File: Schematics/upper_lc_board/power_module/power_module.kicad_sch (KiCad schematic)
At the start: 25 parts, among them U4 PMUX_TPS2121RUXR

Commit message: temp commit for layout work
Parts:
- C10, C12, C13, C9: footprint (none) -> Capacitor_SMD:C_0603_1608Metric
- R11, R12, R25: footprint (none) -> Resistor_SMD:R_0402_1005Metric
- R? (x6): footprint Capacitor_SMD:C_0402_1005Metric -> Resistor_SMD:R_0402_1005Metric
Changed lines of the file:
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@@
 			)
 		)
-		(property "Footprint" ""
+		(property "Footprint" "Capacitor_SMD:C_0603_1608Metric"
 			(at 130.5052 63.5 0)
 			(effects
@@
 			)
 		)
-		(property "Footprint" "Capacitor_SMD:C_0402_1005Metric"
+		(property "Footprint" "Resistor_SMD:R_0402_1005Metric"
 			(at 192.532 139.7 90)
 			(effects
@@
 			)
 		)
-		(property "Footprint" "Capacitor_SMD:C_0402_1005Metric"
+		(property "Footprint" "Resistor_SMD:R_0402_1005Metric"
 			(at 118.618 163.83 90)
 			(effects
@@
 			)
 		)
-		(property "Footprint" "Capacitor_SMD:C_0402_1005Metric"
+		(property "Footprint" "Resistor_SMD:R_0402_1005Metric"
 			(at 192.532 132.08 90)
 			(effects
@@
 			)
 		)
-		(property "Footprint" ""
+		(property "Footprint" "Resistor_SMD:R_0402_1005Metric"
 			(at 123.952 97.79 90)
 			(effects
@@
 			)
 		)
-		(property "Footprint" "Capacitor_SMD:C_0402_1005Metric"
+		(property "Footprint" "Resistor_SMD:R_0402_1005Metric"
 			(at 203.708 124.46 90)
 			(effects
@@
 			)
 		)
-		(property "Footprint" ""
+		(property "Footprint" "Capacitor_SMD:C_0603_1608Metric"
 			(at 137.4648 86.36 0)
 			(effects
@@
 			)
 		)
-		(property "Footprint" "Capacitor_SMD:C_0402_1005Metric"
+		(property "Footprint" "Resistor_SMD:R_0402_1005Metric"
 			(at 118.618 140.97 90)
 			(effects
@@
 			)
 		)
-		(property "Footprint" ""
+		(property "Footprint" "Capacitor_SMD:C_0603_1608Metric"
 			(at 191.4652 63.5 0)
 			(effects
@@
 			)
 		)
-		(property "Footprint" ""
+		(property "Footprint" "Resistor_SMD:R_0402_1005Metric"
 			(at 150.622 92.71 90)
 			(effects
@@
 			)
 		)
-		(property "Footprint" "Capacitor_SMD:C_0402_1005Metric"
+		(property "Footprint" "Resistor_SMD:R_0402_1005Metric"
 			(at 118.618 120.65 90)
 			(effects
@@
 			)
 		)
-		(property "Footprint" ""
+		(property "Footprint" "Capacitor_SMD:C_0603_1608Metric"
 			(at 130.5052 73.66 0)
 			(effects
@@
 			)
 		)
-		(property "Footprint" ""
+		(property "Footprint" "Resistor_SMD:R_0402_1005Metric"
 			(at 123.952 85.09 90)
 			(effects

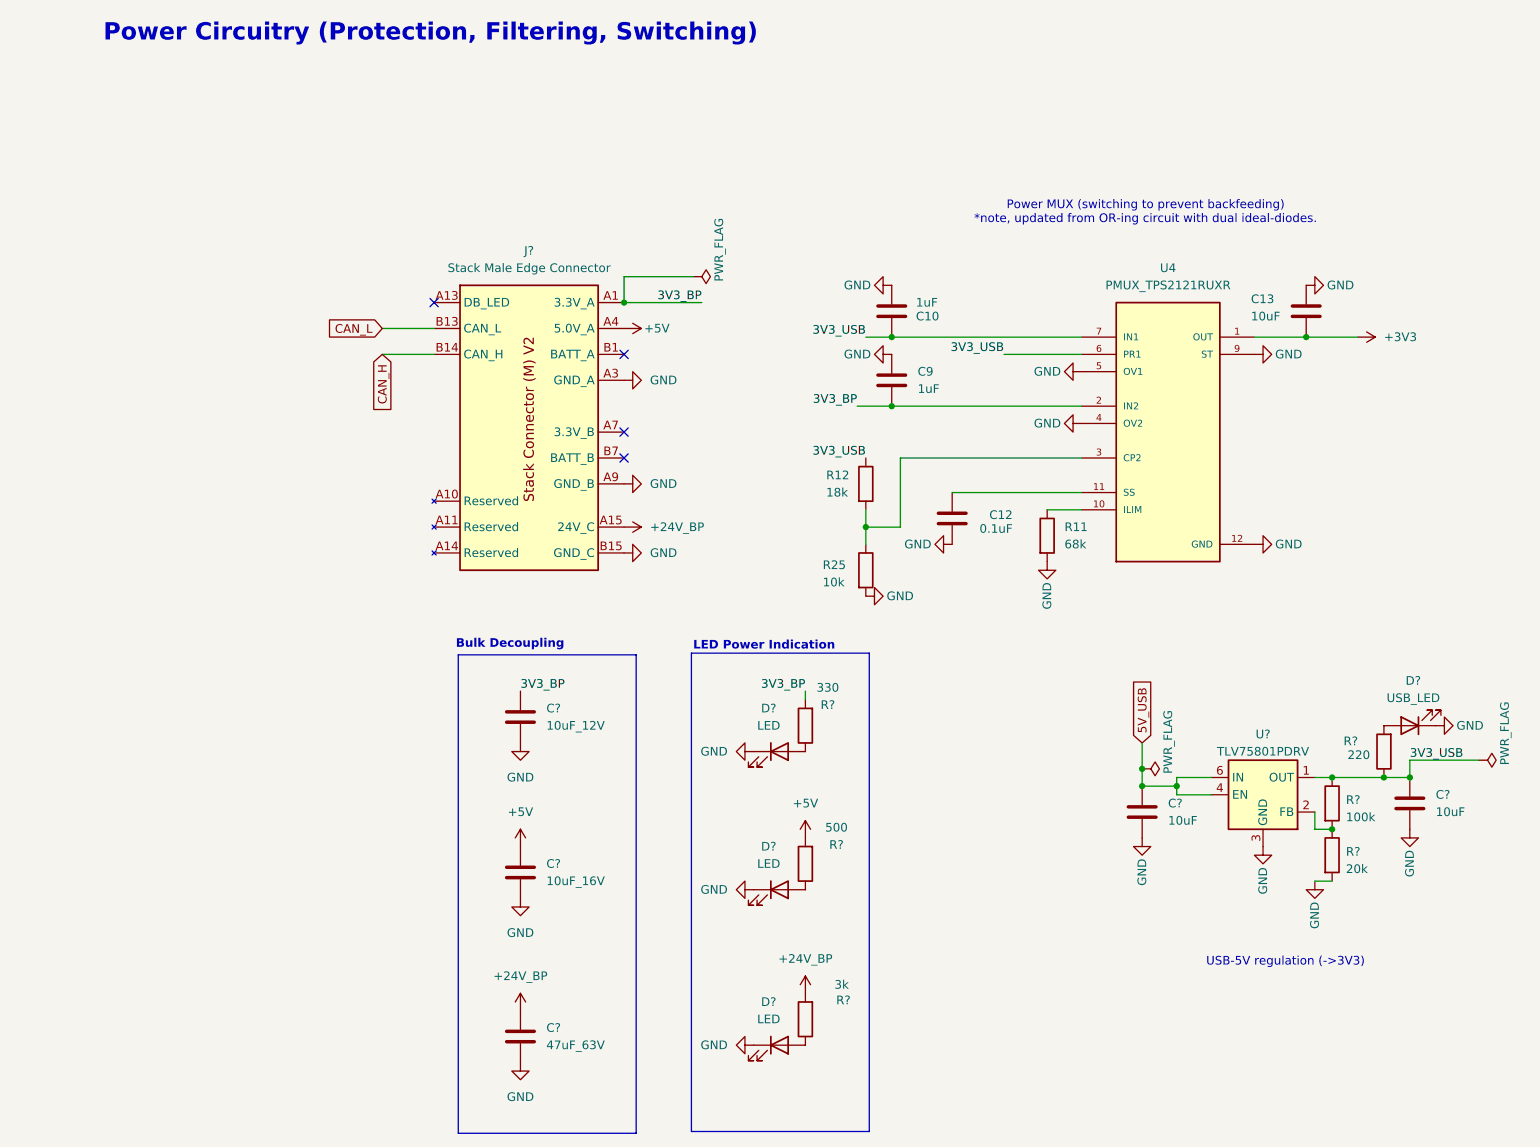
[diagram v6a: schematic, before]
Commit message: revise & organize some circuitry, next: replace MUX with ideal diodes, finish layout, rename GPIO labels for clarity
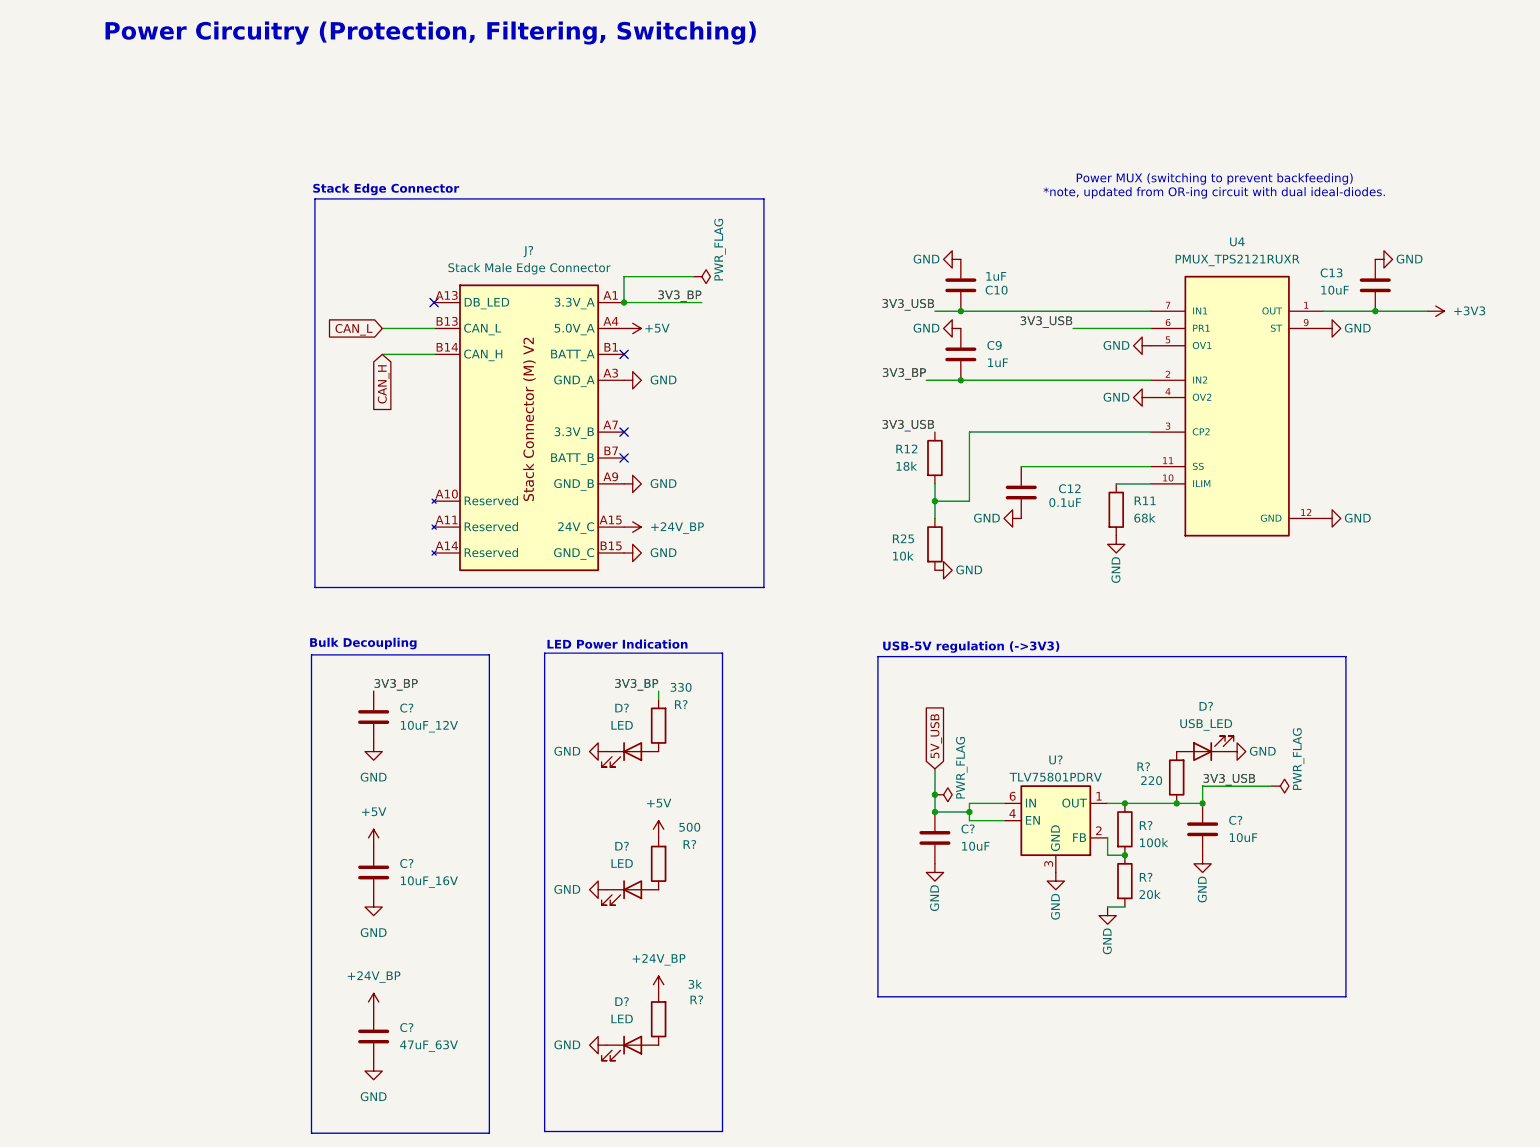
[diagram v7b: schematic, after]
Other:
- note added: "Stack Edge Connector"
- moved on the sheet: C10, C12, C13, C9, C?, D?, R11, R12, R25, R?, U4, U?

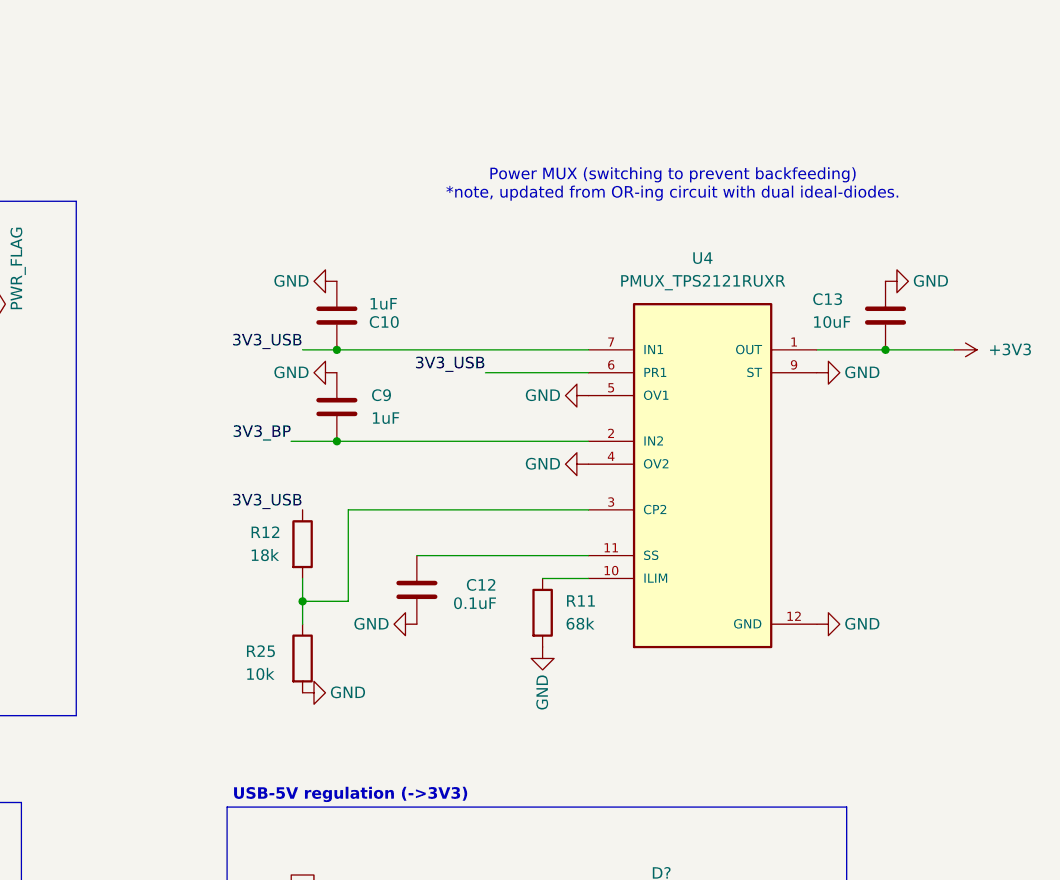
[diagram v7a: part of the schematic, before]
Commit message: add vertical connectors, revert MUX circuitry to ORing setup w ideal diodes
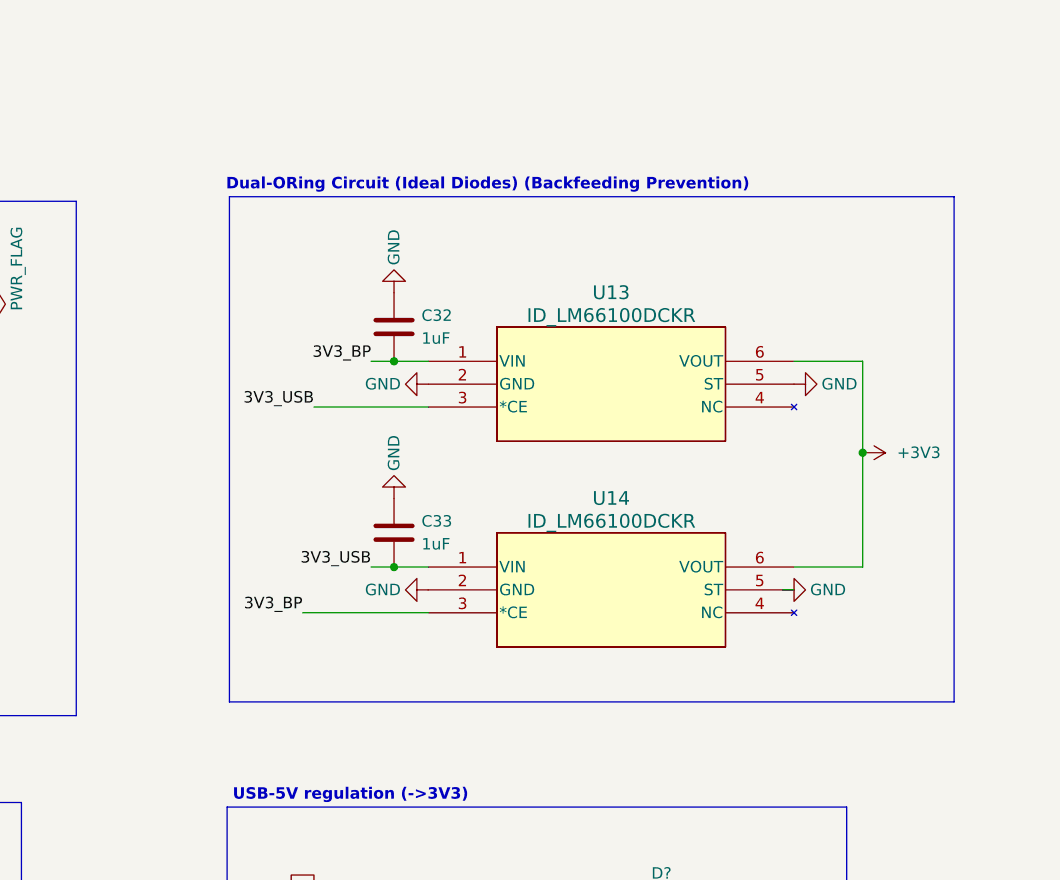
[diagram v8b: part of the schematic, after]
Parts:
- removed C10, C9: 1uF, Capacitor_SMD:C_0603_1608Metric, symbol Device:C
- removed C12: 0.1uF, Capacitor_SMD:C_0603_1608Metric, symbol Device:C
- removed C13: 10uF, Capacitor_SMD:C_0603_1608Metric, symbol Device:C
- removed R11: 68k, Resistor_SMD:R_0402_1005Metric, symbol Device:R
- removed R12: 18k, Resistor_SMD:R_0402_1005Metric, symbol Device:R
- removed R25: 10k, Resistor_SMD:R_0402_1005Metric, symbol Device:R
- removed U4: PMUX_TPS2121RUXR, TPS2121RUXR:IC_TPS2121RUXR, symbol TPS2121RUXR:TPS2121RUXR
- added C32, C33: 1uF, Capacitor_SMD:C_0603_1608Metric, symbol Device:C
- added U13, U14: ID_LM66100DCKR, LM66100:SC-70-6, symbol QRET_Buck_PSU:LM66100DCKR
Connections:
- net +3V3: now also U13.6 (VOUT), U14.6 (VOUT)
- net 3V3_BP: now also C32.1, U13.1 (VIN), U14.3 (*CE)
- net 3V3_USB: now also C33.1, U13.3 (*CE), U14.1 (VIN)
- net GND: now also C32.2, C33.2, U13.2 (GND), U13.5 (ST), U14.2 (GND), U14.5 (ST)
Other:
- note added: "Dual-ORing Circuit (Ideal Diodes) (Backfeeding Prevention)"
- note removed: "Power MUX (switching to prevent backfeeding) *note, updated from OR-ing circuit with dual ideal-diodes."
